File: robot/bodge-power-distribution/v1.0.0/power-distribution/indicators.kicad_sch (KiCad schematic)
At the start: 13 parts, among them Q5 BSS138K, Q6 BSS138K, Q7 BSS138K

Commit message: Sync
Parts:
- renumbered D4 to D5, D5 to D6, D6 to D7, D7 to D8, R32 to R33, R33 to R34, R34 to R36, R35 to R37, R36 to R38
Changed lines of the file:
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@@
     (stroke (width 0) (type default) (color 0 0 0 0))
   )
-  (polyline (pts (xy 13.97 111.76) (xy 199.39 111.76))
+  (polyline (pts (xy 13.97 149.86) (xy 199.39 149.86))
     (stroke (width 0) (type dash) (color 0 0 0 0))
   )
@@
     (stroke (width 0) (type default) (color 0 0 0 0))
   )
-  (polyline (pts (xy 13.97 13.97) (xy 13.97 111.76))
+  (polyline (pts (xy 13.97 13.97) (xy 13.97 149.86))
     (stroke (width 0) (type dash) (color 0 0 0 0))
   )
@@
     (stroke (width 0) (type default) (color 0 0 0 0))
   )
-  (polyline (pts (xy 199.39 111.76) (xy 199.39 13.97))
+  (polyline (pts (xy 199.39 149.86) (xy 199.39 13.97))
     (stroke (width 0) (type dash) (color 0 0 0 0))
   )
@@
   (symbol (lib_id "power:GND") (at 83.82 80.01 0) (unit 1)
     (in_bom yes) (on_board yes) (fields_autoplaced)
-    (property "Reference" "#PWR083" (id 0) (at 83.82 86.36 0)
+    (property "Reference" "#PWR087" (id 0) (at 83.82 86.36 0)
       (effects (font (size 1.27 1.27)) hide)
     )
@@
   (symbol (lib_id "power:GND") (at 127 80.01 0) (unit 1)
     (in_bom yes) (on_board yes) (fields_autoplaced)
-    (property "Reference" "#PWR085" (id 0) (at 127 86.36 0)
+    (property "Reference" "#PWR089" (id 0) (at 127 86.36 0)
       (effects (font (size 1.27 1.27)) hide)
     )
@@
   (symbol (lib_id "power:GND") (at 31.75 43.18 0) (unit 1)
     (in_bom yes) (on_board yes) (fields_autoplaced)
-    (property "Reference" "#PWR078" (id 0) (at 31.75 49.53 0)
+    (property "Reference" "#PWR081" (id 0) (at 31.75 49.53 0)
       (effects (font (size 1.27 1.27)) hide)
     )
@@
   (symbol (lib_id "Device:R_Small_US") (at 58.42 27.94 0) (unit 1)
     (in_bom yes) (on_board yes) (fields_autoplaced)
-    (property "Reference" "R34" (id 0) (at 60.96 26.6699 0)
+    (property "Reference" "R36" (id 0) (at 60.96 26.6699 0)
       (effects (font (size 1.27 1.27)) (justify left))
     )
@@
   (symbol (lib_id "power:GND") (at 58.42 43.18 0) (unit 1)
     (in_bom yes) (on_board yes) (fields_autoplaced)
-    (property "Reference" "#PWR081" (id 0) (at 58.42 49.53 0)
+    (property "Reference" "#PWR085" (id 0) (at 58.42 49.53 0)
       (effects (font (size 1.27 1.27)) hide)
     )
@@
   (symbol (lib_id "AT-Supplies:+V_{BATT(PROTECTED)}") (at 127 57.15 0) (unit 1)
     (in_bom no) (on_board no) (fields_autoplaced)
-    (property "Reference" "#PWR084" (id 0) (at 127 60.96 0)
+    (property "Reference" "#PWR088" (id 0) (at 127 60.96 0)
       (effects (font (size 1.27 1.27)) hide)
     )
@@
   (symbol (lib_id "Device:LED") (at 99.06 72.39 90) (unit 1)
     (in_bom yes) (on_board yes) (fields_autoplaced)
-    (property "Reference" "D6" (id 0) (at 102.87 72.7074 90)
+    (property "Reference" "D7" (id 0) (at 102.87 72.7074 90)
       (effects (font (size 1.27 1.27)) (justify right))
     )
@@
   (symbol (lib_id "Device:LED") (at 58.42 36.83 90) (unit 1)
     (in_bom yes) (on_board yes) (fields_autoplaced)
-    (property "Reference" "D5" (id 0) (at 62.23 37.1474 90)
+    (property "Reference" "D6" (id 0) (at 62.23 37.1474 90)
       (effects (font (size 1.27 1.27)) (justify right))
     )
@@
   (symbol (lib_id "AT-Supplies:+V_{BATT(PROTECTED)}") (at 40.64 57.15 0) (unit 1)
     (in_bom no) (on_board no) (fields_autoplaced)
-    (property "Reference" "#PWR079" (id 0) (at 40.64 60.96 0)
+    (property "Reference" "#PWR082" (id 0) (at 40.64 60.96 0)
       (effects (font (size 1.27 1.27)) hide)
     )
@@
   (symbol (lib_id "Device:R_Small_US") (at 40.64 62.23 0) (unit 1)
     (in_bom yes) (on_board yes) (fields_autoplaced)
-    (property "Reference" "R33" (id 0) (at 43.18 60.9599 0)
+    (property "Reference" "R34" (id 0) (at 43.18 60.9599 0)
       (effects (font (size 1.27 1.27)) (justify left))
     )
@@
   (symbol (lib_id "Device:R_Small_US") (at 83.82 62.23 0) (unit 1)
     (in_bom yes) (on_board yes) (fields_autoplaced)
-    (property "Reference" "R35" (id 0) (at 86.36 60.9599 0)
+    (property "Reference" "R37" (id 0) (at 86.36 60.9599 0)
       (effects (font (size 1.27 1.27)) (justify left))
     )
@@
   (symbol (lib_id "Device:R_Small_US") (at 127 62.23 0) (unit 1)
     (in_bom yes) (on_board yes) (fields_autoplaced)
-    (property "Reference" "R36" (id 0) (at 129.54 60.9599 0)
+    (property "Reference" "R38" (id 0) (at 129.54 60.9599 0)
       (effects (font (size 1.27 1.27)) (justify left))
     )
@@
   (symbol (lib_id "Device:R_Small_US") (at 31.75 27.94 0) (unit 1)
     (in_bom yes) (on_board yes) (fields_autoplaced)
-    (property "Reference" "R32" (id 0) (at 34.29 26.6699 0)
+    (property "Reference" "R33" (id 0) (at 34.29 26.6699 0)
       (effects (font (size 1.27 1.27)) (justify left))
     )
@@
   (symbol (lib_id "Device:LED") (at 55.88 72.39 90) (unit 1)
     (in_bom yes) (on_board yes) (fields_autoplaced)
-    (property "Reference" "D4" (id 0) (at 59.69 72.7074 90)
+    (property "Reference" "D5" (id 0) (at 59.69 72.7074 90)
       (effects (font (size 1.27 1.27)) (justify right))
     )
@@
   (symbol (lib_id "AT-Supplies:+V_{BATT(PROTECTED)}") (at 83.82 57.15 0) (unit 1)
     (in_bom no) (on_board no) (fields_autoplaced)
-    (property "Reference" "#PWR082" (id 0) (at 83.82 60.96 0)
+    (property "Reference" "#PWR086" (id 0) (at 83.82 60.96 0)
       (effects (font (size 1.27 1.27)) hide)
     )
@@
   (symbol (lib_id "power:GND") (at 40.64 80.01 0) (unit 1)
     (in_bom yes) (on_board yes) (fields_autoplaced)
-    (property "Reference" "#PWR080" (id 0) (at 40.64 86.36 0)
+    (property "Reference" "#PWR083" (id 0) (at 40.64 86.36 0)
       (effects (font (size 1.27 1.27)) hide)
     )
@@
   (symbol (lib_id "Device:LED") (at 142.24 72.39 90) (unit 1)
     (in_bom yes) (on_board yes) (fields_autoplaced)
-    (property "Reference" "D7" (id 0) (at 146.05 72.7074 90)
-      (effects (font (size 1.27 1.27)) (justify right))
-    )
+    (property "Reference" "D8" (id 0) (at 146.05 72.7074 90)
+      (effects (font (size 1.27 1.27)) (justify right))
+    )

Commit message: Sync
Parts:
- added C30, C31: 4.7uF 25V, Capacitor_SMD:C_0603_1608Metric_Pad1.08x0.95mm_HandSolder, symbol Device:C
- added J10: Conn_01x04, symbol Connector_Generic:Conn_01x04
- added U7, U8, U9: SK9822, AT-LED:SK9822, symbol AT-LED:SK9822
- renumbered D5 to D4, D6 to D5, D7 to D6, D8 to D7, R36 to R35, R37 to R36, R38 to R37
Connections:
- net GND: now also C30.1, C31.1, J10.4 (Pin_4), U7.3 (GND), U8.3 (GND), U9.3 (GND)
- new net: U8.6 (SDO), U9.1 (SDI)
- new net: U8.5 (CKO), U9.2 (CKI)
- new net: U7.5 (CKO), U8.2 (CKI)
- new net: U7.6 (SDO), U8.1 (SDI)
- new net +5V: C30.2, C31.2, J10.1 (Pin_1), U7.4 (VCC), U8.4 (VCC), U9.4 (VCC)
- new net DOTSTAR.CLK: U7.2 (CKI)
- new net DOTSTAR.DAT: U7.1 (SDI)
- new net DOTSTAR_{EXT}.CLK: J10.3 (Pin_3), U9.5 (CKO)
- new net DOTSTAR_{EXT}.DAT: J10.2 (Pin_2), U9.6 (SDO)

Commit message: Sync
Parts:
- added D3, D5, D6, D9: Green, AT-LED:LED0603, symbol Device:LED
- added R35, R38, R39, R41: 10k, Resistor_SMD:R_0402_1005Metric_Pad0.72x0.64mm_HandSolder, symbol Device:R_Small_US
- J10: footprint (none) -> Connector_PinSocket_2.54mm:PinSocket_1x04_P2.54mm_Vertical
- renumbered D6 to D10, D7 to D11, D3 to D4, D4 to D7, D5 to D8, R33 to R36, R34 to R37, R35 to R40, R36 to R42, R37 to R43
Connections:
- net DOTSTAR_{EXT}.CLK: now also J10.2 (Pin_2); no longer J10.3 (Pin_3)
- net DOTSTAR_{EXT}.DAT: now also J10.3 (Pin_3); no longer J10.2 (Pin_2)
- net GND: now also D3.1 (K), D5.1 (K), D6.1 (K), D9.1 (K)
- new net: D9.2 (A), R41.2
- new net: D3.2 (A), R35.2
- new net: D6.2 (A), R39.2
- new net: D5.2 (A), R38.2
- new net LED0: R35.1
- new net LED1: R38.1
- new net LED2: R39.1
- new net LED3: R41.1

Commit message: Alpha (0.0.0)
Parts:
- C32: renamed from C30; footprint Capacitor_SMD:C_0603_1608Metric_Pad1.08x0.95mm_HandSolder -> Capacitor_SMD:C_0805_2012Metric
- C33: renamed from C31; footprint Capacitor_SMD:C_0603_1608Metric_Pad1.08x0.95mm_HandSolder -> Capacitor_SMD:C_0805_2012Metric
- renumbered D8 to D10, D9 to D11, D10 to D12, D11 to D13, D3 to D5, D4 to D6, D5 to D7, D6 to D8, D7 to D9, J10 to J20, Q5 to Q6, Q6 to Q7, Q7 to Q8, R35 to R39, R36 to R40, R37 to R41, R38 to R42, R39 to R43, R40 to R44, R41 to R45, R42 to R46, R43 to R47, U9 to U10, U7 to U8, U8 to U9

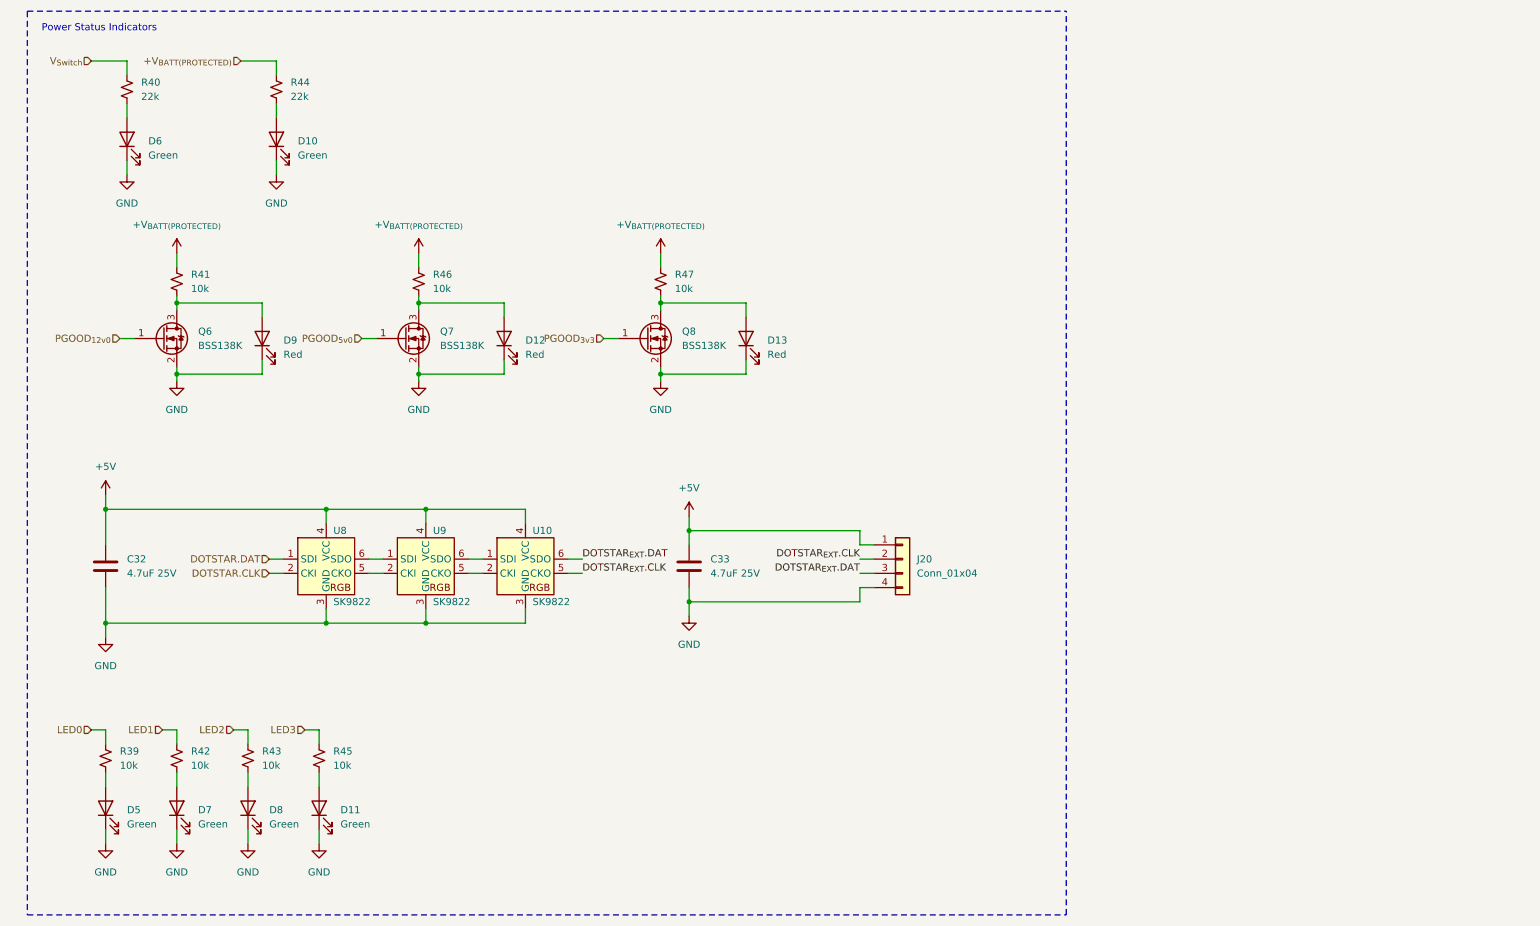
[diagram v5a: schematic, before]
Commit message: Minor aesthetics update; added 4 Green/Red LEDs for the dot pattern preview
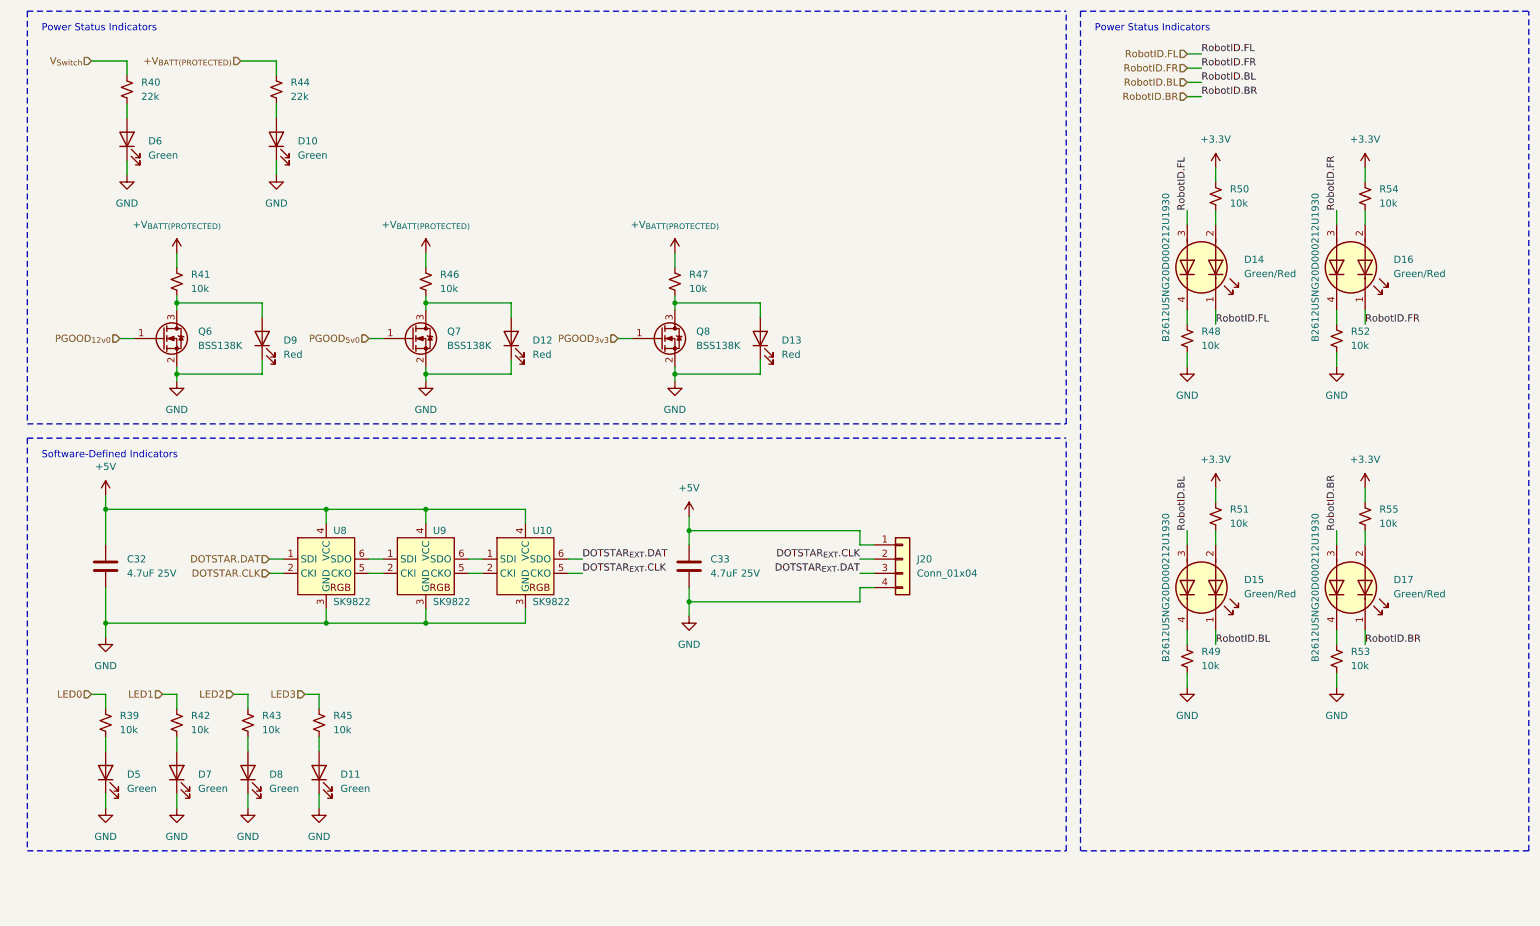
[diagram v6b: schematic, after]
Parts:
- added D14, D15, D16, D17: Green/Red, AT-LED:LED0606_CCW, symbol AT-LED:LED_Dual_KAAK
- added R48, R49, R50, R51, R52, R53, R54, R55: 10k, Resistor_SMD:R_0402_1005Metric_Pad0.72x0.64mm_HandSolder, symbol Device:R_Small_US
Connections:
- net GND: now also R48.1, R49.1, R52.1, R53.1
- new net: D15.4 (K2), R49.2
- new net: D17.4 (K2), R53.2
- new net: D15.2 (A1), R51.1
- new net: D17.2 (A1), R55.1
- new net: D14.2 (A1), R50.1
- new net: D16.4 (K2), R52.2
- new net: D16.2 (A1), R54.1
- new net: D14.4 (K2), R48.2
- new net +3.3V: R50.2, R51.2, R54.2, R55.2
- new net RobotID.BL: D15.1 (K1), D15.3 (A2)
- new net RobotID.BR: D17.1 (K1), D17.3 (A2)
- new net RobotID.FL: D14.1 (K1), D14.3 (A2)
- new net RobotID.FR: D16.1 (K1), D16.3 (A2)
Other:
- note added: "Software-Defined Indicators"
- moved on the sheet: D11, D12, D13, D5, D7, D8, Q7, Q8, R39, R42, R43, R45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

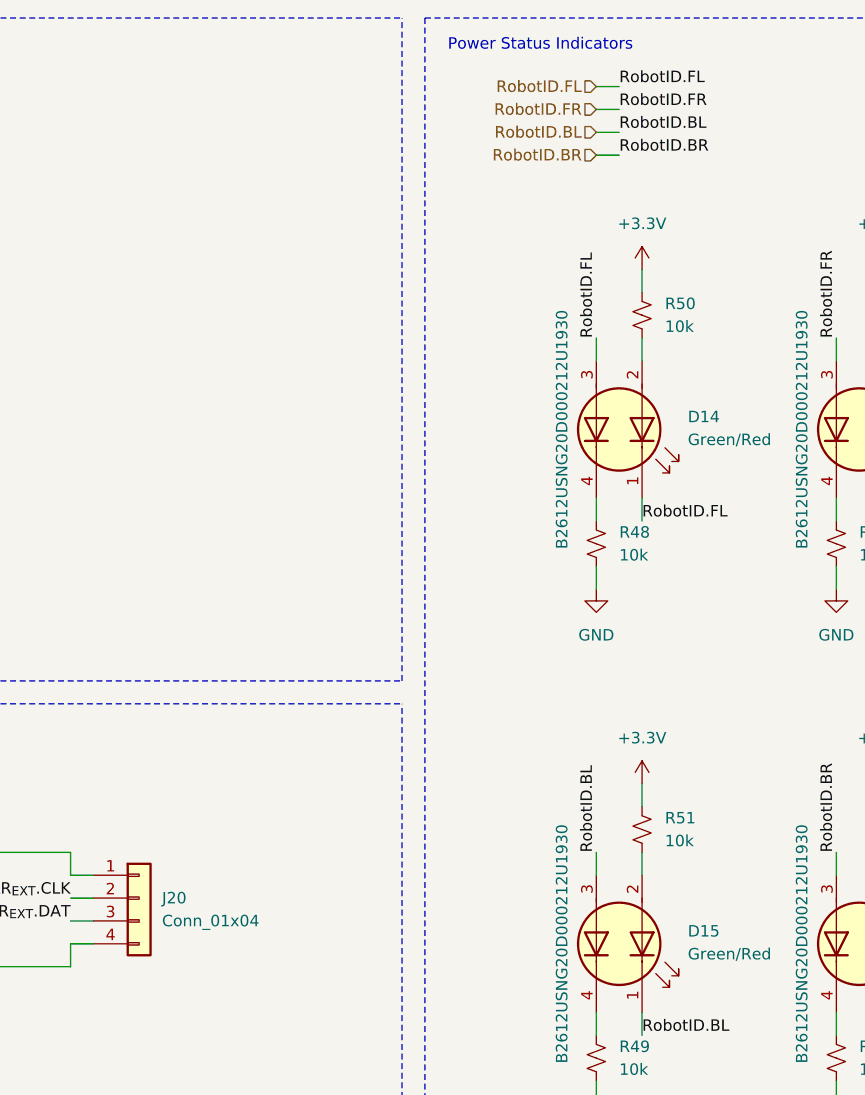
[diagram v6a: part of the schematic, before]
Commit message: Schematic aesthetics & formatting
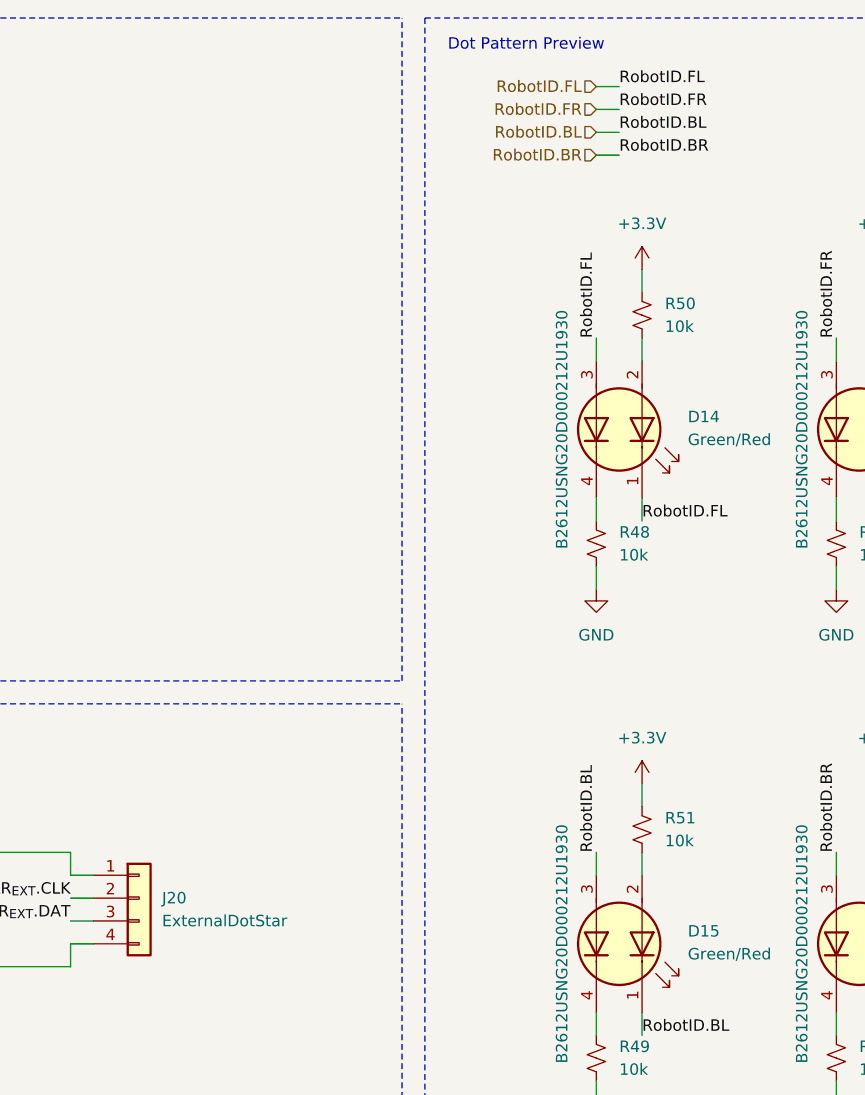
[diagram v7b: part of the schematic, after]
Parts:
- J20: value Conn_01x04 -> ExternalDotStar; now left out of the parts list
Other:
- note added: "Dot Pattern Preview"
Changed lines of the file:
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@@
     (effects (font (size 1.27 1.27)) (justify left bottom))
   )
-  (text "Power Status Indicators" (at 204.47 17.78 0)
+  (text "Dot Pattern Preview" (at 204.47 17.78 0)
     (effects (font (size 1.27 1.27)) (justify left bottom))
   )
@@
   )
   (symbol (lib_id "Connector_Generic:Conn_01x04") (at 170.18 111.76 0) (unit 1)
-    (in_bom yes) (on_board yes) (fields_autoplaced)
+    (in_bom no) (on_board yes) (fields_autoplaced)
     (property "Reference" "J20" (id 0) (at 172.72 111.7599 0)
       (effects (font (size 1.27 1.27)) (justify left))
     )
-    (property "Value" "Conn_01x04" (id 1) (at 172.72 114.2999 0)
-      (effects (font (size 1.27 1.27)) (justify left))
-    )
+    (property "Value" "ExternalDotStar" (id 1) (at 172.72 114.2999 0)
+      (effects (font (size 1.27 1.27)) (justify left))
+    )

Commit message: Prepare files for production
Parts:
- R51: renamed from R39; footprint Resistor_SMD:R_0402_1005Metric_Pad0.72x0.64mm_HandSolder -> Resistor_SMD:R_0402_1005Metric
- R52: renamed from R40; footprint Resistor_SMD:R_0402_1005Metric_Pad0.72x0.64mm_HandSolder -> Resistor_SMD:R_0402_1005Metric
- R53: renamed from R41; footprint Resistor_SMD:R_0402_1005Metric_Pad0.72x0.64mm_HandSolder -> Resistor_SMD:R_0402_1005Metric
- R54: renamed from R42; footprint Resistor_SMD:R_0402_1005Metric_Pad0.72x0.64mm_HandSolder -> Resistor_SMD:R_0402_1005Metric
- R55: renamed from R43; footprint Resistor_SMD:R_0402_1005Metric_Pad0.72x0.64mm_HandSolder -> Resistor_SMD:R_0402_1005Metric
- R56: renamed from R44; footprint Resistor_SMD:R_0402_1005Metric_Pad0.72x0.64mm_HandSolder -> Resistor_SMD:R_0402_1005Metric
- R57: renamed from R45; footprint Resistor_SMD:R_0402_1005Metric_Pad0.72x0.64mm_HandSolder -> Resistor_SMD:R_0402_1005Metric
- R58: renamed from R46; footprint Resistor_SMD:R_0402_1005Metric_Pad0.72x0.64mm_HandSolder -> Resistor_SMD:R_0402_1005Metric
- R59: renamed from R47; footprint Resistor_SMD:R_0402_1005Metric_Pad0.72x0.64mm_HandSolder -> Resistor_SMD:R_0402_1005Metric
- R60: renamed from R48; footprint Resistor_SMD:R_0402_1005Metric_Pad0.72x0.64mm_HandSolder -> Resistor_SMD:R_0402_1005Metric
- R61: renamed from R49; footprint Resistor_SMD:R_0402_1005Metric_Pad0.72x0.64mm_HandSolder -> Resistor_SMD:R_0402_1005Metric
- R62: renamed from R50; footprint Resistor_SMD:R_0402_1005Metric_Pad0.72x0.64mm_HandSolder -> Resistor_SMD:R_0402_1005Metric
- R63: renamed from R51; footprint Resistor_SMD:R_0402_1005Metric_Pad0.72x0.64mm_HandSolder -> Resistor_SMD:R_0402_1005Metric
- R64: renamed from R52; footprint Resistor_SMD:R_0402_1005Metric_Pad0.72x0.64mm_HandSolder -> Resistor_SMD:R_0402_1005Metric
- R65: renamed from R53; footprint Resistor_SMD:R_0402_1005Metric_Pad0.72x0.64mm_HandSolder -> Resistor_SMD:R_0402_1005Metric
- R66: renamed from R54; footprint Resistor_SMD:R_0402_1005Metric_Pad0.72x0.64mm_HandSolder -> Resistor_SMD:R_0402_1005Metric
- R67: renamed from R55; footprint Resistor_SMD:R_0402_1005Metric_Pad0.72x0.64mm_HandSolder -> Resistor_SMD:R_0402_1005Metric
- renumbered C32 to C36, C33 to C37
